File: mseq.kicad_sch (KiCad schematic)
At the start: 87 parts, among them J1 Screen_I2C, J3 Conn_ARM_JTAG_SWD_10, SW1 RESET, SW2 ON/OFF, SW3 MS/SLAVE, SW4 BOOT, U1 SN74HCT125DR, U2 H11L1M, U3 AMS1117-3.3, U4 STM32F413CHUx, U5 CP2102N-Axx-xQFN20, U6 H11L1M, U7 W25Q16JVSS, U8 MB85RS256B, Y1 32.768kHz ±20ppm 6pF, Y2 25 MHz ±20ppm 18pF

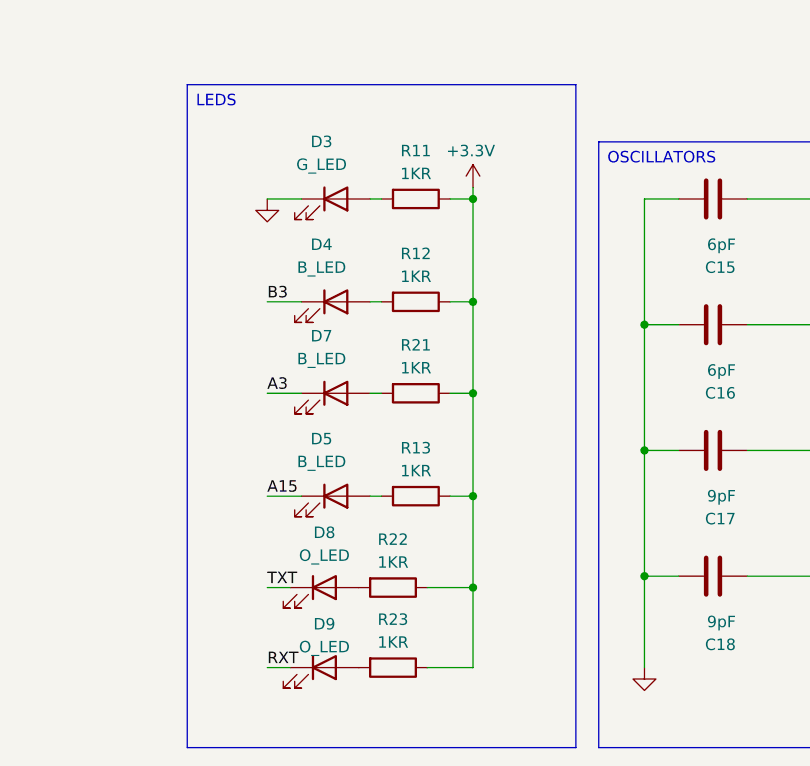
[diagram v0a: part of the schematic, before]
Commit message: Balance LED brightness, align screen header, pin footprint libraries
- LED series resistors re-sized for roughly equal brightness (~30 mcd):
  R11 green 1k -> 3.9k (C17614), R12/R13/R21 blue 1k -> 390R (C17655),
  R22/R23 orange 1k -> 1.5k (C4310); all UNI-ROYAL 0805 basic parts
- J1 (screen I2C header) moved to y=98.31 so its pins match the
  HS242L03B2C01 OLED module drawing (centred between the 68x39 mm holes)
- fp-lib-table: list the KiCad standard footprint libraries used by the
  board (via ${KICAD10_FOOTPRINT_DIR}) so they are enabled for everyone
- PCB layout work in progress

Co-Authored-By: Claude Opus 5.5 <noreply@anthropic.com>
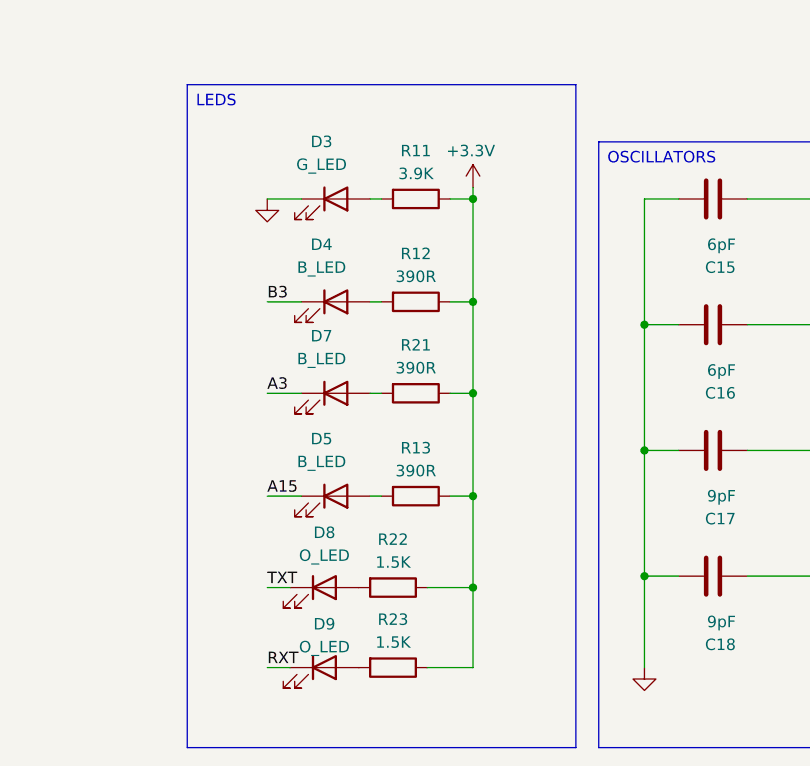
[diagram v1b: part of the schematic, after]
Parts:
- R11: value 1KR -> 3.9K; LCSC C17513 -> C17614; MPN 0805W8F1001T5E -> 0805W8F3901T5E
- R12, R13, R21: value 1KR -> 390R; LCSC C17513 -> C17655; MPN 0805W8F1001T5E -> 0805W8F3900T5E
- R22, R23: value 1KR -> 1.5K; LCSC C17513 -> C4310; MPN 0805W8F1001T5E -> 0805W8F1501T5E
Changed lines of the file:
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@@
 			)
 		)
-		(property "Value" "1KR"
+		(property "Value" "3.9K"
 			(at 166.37 219.456 90)
 			(show_name no)
@@
 			)
 		)
-		(property "MPN" "0805W8F1001T5E"
+		(property "MPN" "0805W8F3901T5E"
 			(at 166.37 222.25 90)
 			(hide yes)
@@
 			)
 		)
-		(property "LCSC" "C17513"
+		(property "LCSC" "C17614"
 			(at 166.37 222.25 90)
 			(hide yes)
@@
 			)
 		)
-		(property "Value" "1KR"
+		(property "Value" "390R"
 			(at 166.37 230.886 90)
 			(show_name no)
@@
 			)
 		)
-		(property "MPN" "0805W8F1001T5E"
+		(property "MPN" "0805W8F3900T5E"
 			(at 166.37 233.68 90)
 			(hide yes)
@@
 			)
 		)
-		(property "LCSC" "C17513"
+		(property "LCSC" "C17655"
 			(at 166.37 233.68 90)
 			(hide yes)
@@
 			)
 		)
-		(property "Value" "1KR"
+		(property "Value" "390R"
 			(at 166.37 252.476 90)
 			(show_name no)
@@
 			)
 		)
-		(property "MPN" "0805W8F1001T5E"
+		(property "MPN" "0805W8F3900T5E"
 			(at 166.37 255.27 90)
 			(hide yes)
@@
 			)
 		)
-		(property "LCSC" "C17513"
+		(property "LCSC" "C17655"
 			(at 166.37 255.27 90)
 			(hide yes)
@@
 			)
 		)
-		(property "Value" "1KR"
+		(property "Value" "1.5K"
 			(at 163.83 262.636 90)
 			(show_name no)
@@
 			)
 		)
-		(property "MPN" "0805W8F1001T5E"
+		(property "MPN" "0805W8F1501T5E"
 			(at 163.83 265.43 90)
 			(hide yes)
@@
 			)
 		)
-		(property "LCSC" "C17513"
+		(property "LCSC" "C4310"
 			(at 163.83 265.43 90)
 			(hide yes)
@@
 			)
 		)
-		(property "Value" "1KR"
+		(property "Value" "390R"
 			(at 166.37 241.046 90)
 			(show_name no)
@@
 			)
 		)
-		(property "MPN" "0805W8F1001T5E"
+		(property "MPN" "0805W8F3900T5E"
 			(at 166.37 243.84 90)
 			(hide yes)
@@
 			)
 		)
-		(property "LCSC" "C17513"
+		(property "LCSC" "C17655"
 			(at 166.37 243.84 90)
 			(hide yes)
@@
 			)
 		)
-		(property "Value" "1KR"
+		(property "Value" "1.5K"
 			(at 163.83 271.526 90)
 			(show_name no)
@@
 			)
 		)
-		(property "MPN" "0805W8F1001T5E"
+		(property "MPN" "0805W8F1501T5E"
 			(at 163.83 274.32 90)
 			(hide yes)
@@
 			)
 		)
-		(property "LCSC" "C17513"
+		(property "LCSC" "C4310"
 			(at 163.83 274.32 90)
 			(hide yes)

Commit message: Screen header: switch J1 to 5.7 mm female socket
Replace the 8.5 mm BOOMELE socket (C2718488) with the hanxia
HX PM2.54-1x4P ZC H5.7 (C46061763) to lower the screen stack-up.
Use the PinSocket_1x04 footprint instead of the male PinHeader one
(identical pads) and add Connector_PinSocket_2.54mm to fp-lib-table.

Co-Authored-By: Claude Opus 5.5 <noreply@anthropic.com>
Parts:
- J1: footprint Connector_PinHeader_2.54mm:PinHeader_1x04_P2.54mm_Vertical -> Connector_PinSocket_2.54mm:PinSocket_1x04_P2.54mm_Vertical; LCSC C2718488 -> C46061763; MPN 2.54-1*4P -> HX PM2.54-1x4P ZC H5.7
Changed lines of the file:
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@@
 			)
 		)
-		(property "Footprint" "Connector_PinHeader_2.54mm:PinHeader_1x04_P2.54mm_Vertical"
+		(property "Footprint" "Connector_PinSocket_2.54mm:PinSocket_1x04_P2.54mm_Vertical"
 			(at 340.36 25.4 0)
 			(hide yes)
@@
 			)
 		)
-		(property "LCSC" "C2718488"
+		(property "LCSC" "C46061763"
 			(at 340.36 25.4 0)
 			(hide yes)
@@
 			)
 		)
-		(property "MPN" "2.54-1*4P"
+		(property "MPN" "HX PM2.54-1x4P ZC H5.7"
 			(at 340.36 25.4 0)
 			(hide yes)
